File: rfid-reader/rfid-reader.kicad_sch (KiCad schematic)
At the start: 14 parts, among them U1 ATmega1284-P, U2 keypad, U3 Interface_RFID_SPI

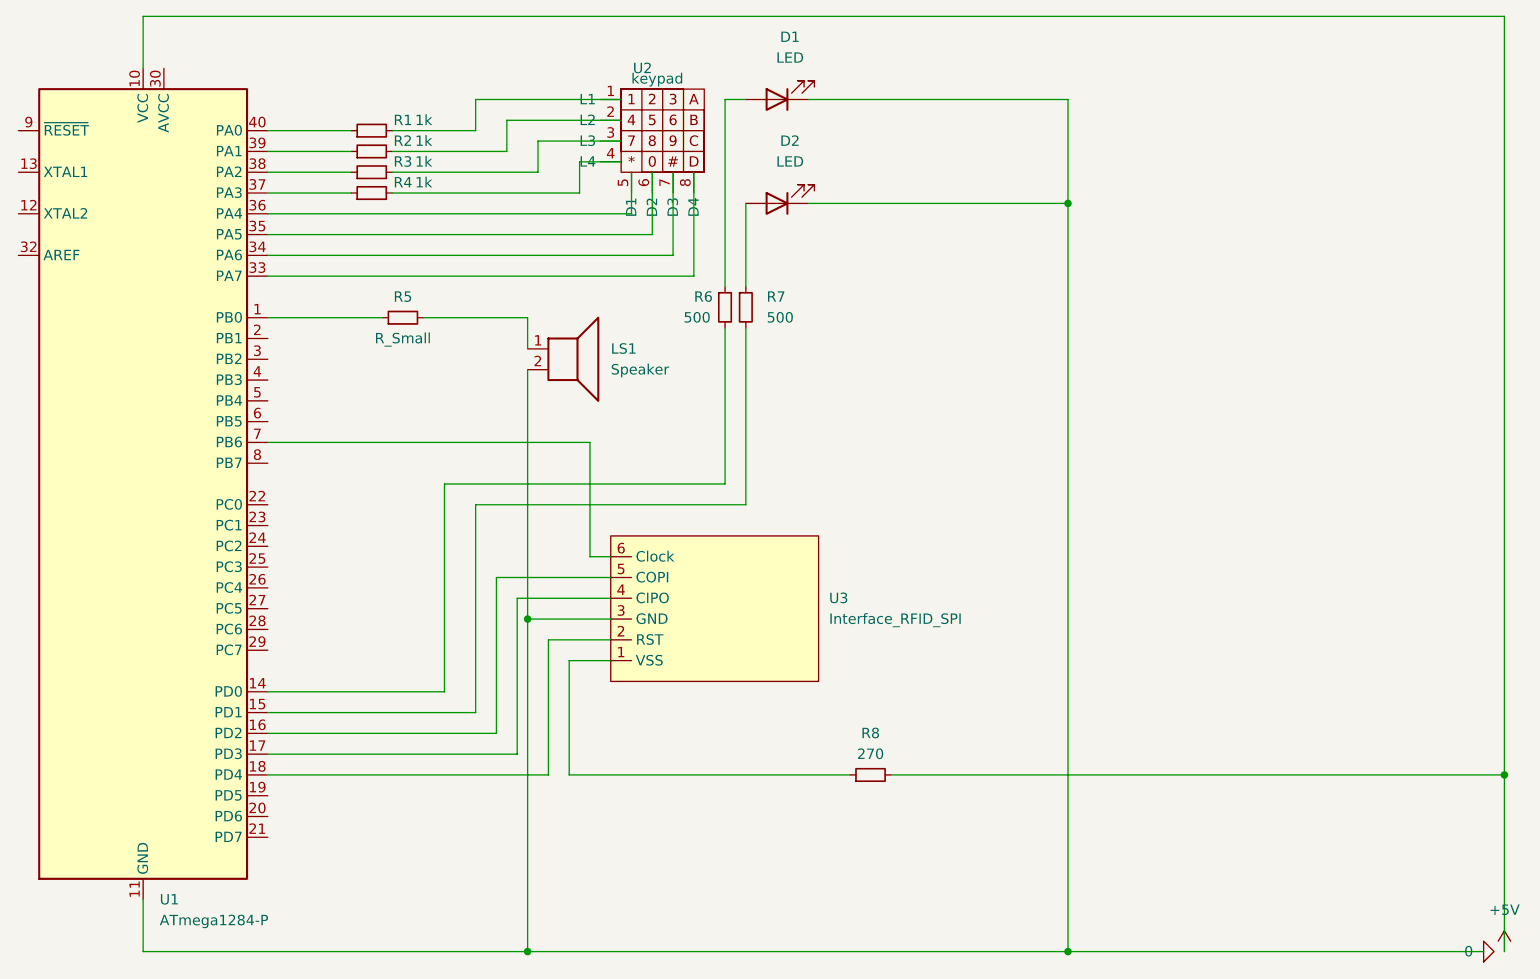
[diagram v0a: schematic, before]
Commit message: Pin configuration is now accurate to reality
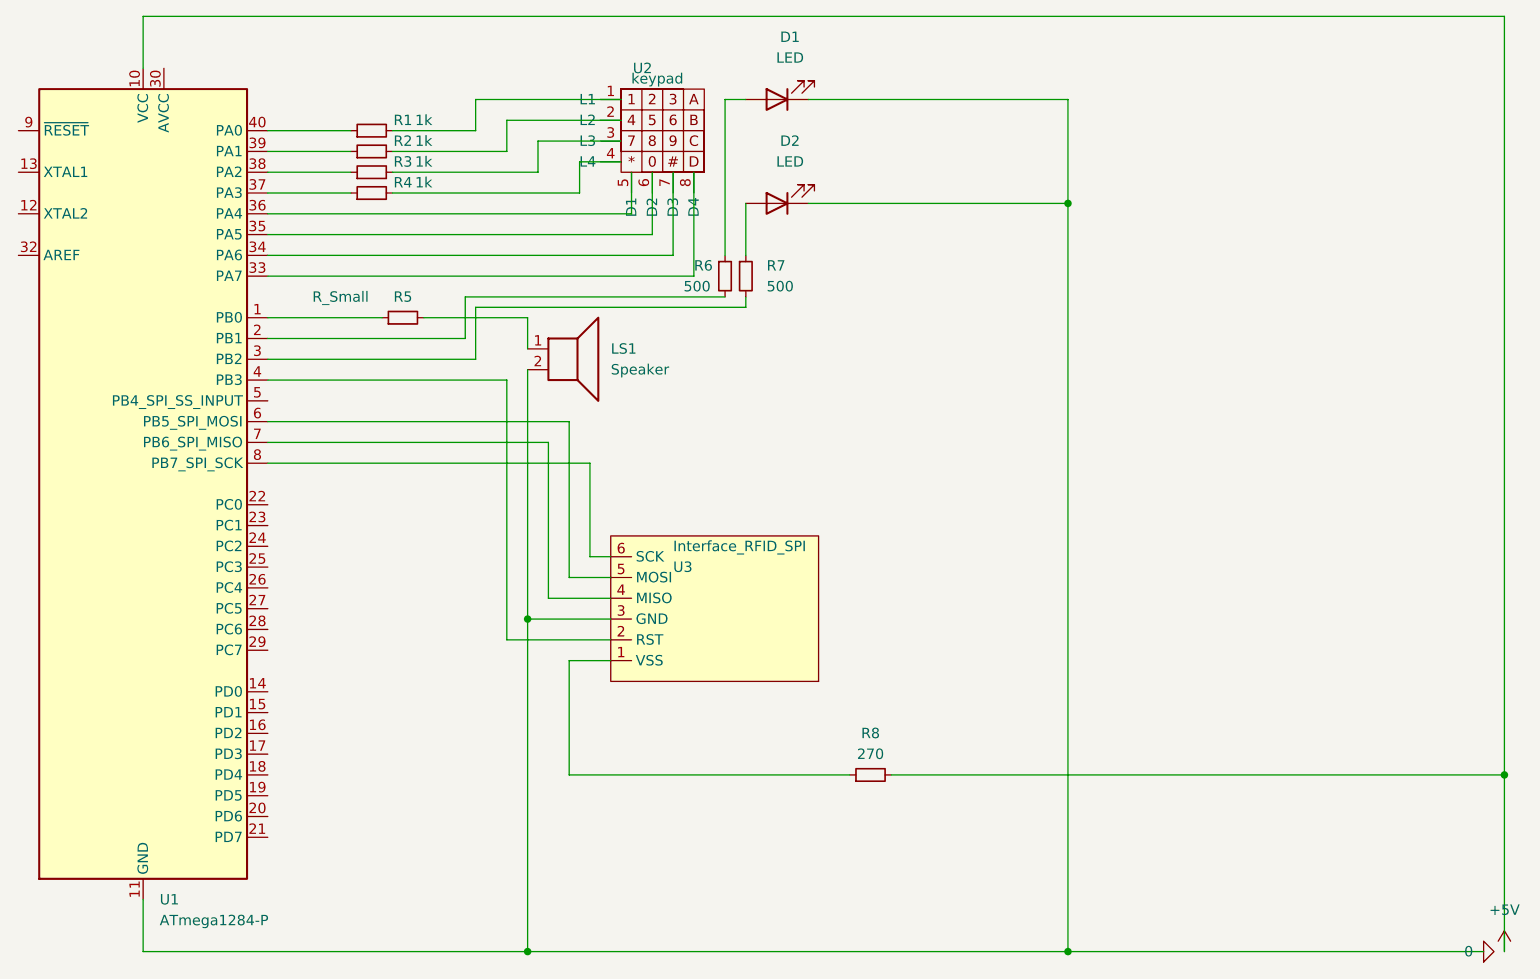
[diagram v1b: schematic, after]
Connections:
- net at U3.2 (RST): now also U1.4 (PB3); no longer U1.18 (PD4)
- net at U3.4 (MISO): now also U1.7 (PB6_SPI_MISO); no longer U1.17 (PD3)
- net at U3.5 (MOSI): now also U1.6 (PB5_SPI_MOSI); no longer U1.16 (PD2)
- net at U3.6 (SCK): now also U1.8 (PB7_SPI_SCK); no longer U1.7 (PB6)
- net at R6.2: now also U1.2 (PB1); no longer U1.14 (PD0)
- net at U1.15 (PD1): no longer R7.2
- net at U1.3 (PB2): now also R7.2
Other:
- moved on the sheet: R6, R7

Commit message: Removed resistors from keypad circuit
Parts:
- removed R1, R2, R3, R4: 1k, symbol Device:R_Small
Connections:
- net at U2.1 (L1): now also U1.40 (PA0)
- net at U2.2 (L2): now also U1.39 (PA1)
- net at U2.3 (L3): now also U1.38 (PA2)
- net at U2.4 (L4): now also U1.37 (PA3)
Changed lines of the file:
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@@
-    (stroke (width 0) (type default) (color 0 0 0 0))
-  )
-  (wire (pts (xy 64.77 34.29) (xy 74.93 34.29))
     (stroke (width 0) (type default) (color 0 0 0 0))
   )
@@
     (stroke (width 0) (type default) (color 0 0 0 0))
   )
-  (wire (pts (xy 80.01 34.29) (xy 93.98 34.29))
+  (wire (pts (xy 64.77 34.29) (xy 93.98 34.29))
     (stroke (width 0) (type default) (color 0 0 0 0))
   )
@@
     (stroke (width 0) (type default) (color 0 0 0 0))
   )
-  (wire (pts (xy 80.01 31.75) (xy 90.17 31.75))
+  (wire (pts (xy 64.77 31.75) (xy 90.17 31.75))
     (stroke (width 0) (type default) (color 0 0 0 0))
   )
@@
     (stroke (width 0) (type default) (color 0 0 0 0))
   )
-  (wire (pts (xy 64.77 31.75) (xy 74.93 31.75))
-    (stroke (width 0) (type default) (color 0 0 0 0))
-  )
   (wire (pts (xy 64.77 44.45) (xy 111.76 44.45))
     (stroke (width 0) (type default) (color 0 0 0 0))
@@
     (stroke (width 0) (type default) (color 0 0 0 0))
   )
-  (wire (pts (xy 80.01 36.83) (xy 97.79 36.83))
+  (wire (pts (xy 64.77 36.83) (xy 97.79 36.83))
     (stroke (width 0) (type default) (color 0 0 0 0))
   )
@@
     (stroke (width 0) (type default) (color 0 0 0 0))
   )
-  (wire (pts (xy 80.01 39.37) (xy 102.87 39.37))
+  (wire (pts (xy 64.77 39.37) (xy 102.87 39.37))
     (stroke (width 0) (type default) (color 0 0 0 0))
   )
@@
     (stroke (width 0) (type default) (color 0 0 0 0))
   )
-  (wire (pts (xy 64.77 36.83) (xy 74.93 36.83))
-    (stroke (width 0) (type default) (color 0 0 0 0))
-  )
   (wire (pts (xy 106.68 93.98) (xy 93.98 93.98))
     (stroke (width 0) (type default) (color 0 0 0 0))
   )
   (wire (pts (xy 162.56 40.64) (xy 162.56 132.08))
-    (stroke (width 0) (type default) (color 0 0 0 0))
-  )
-  (wire (pts (xy 64.77 39.37) (xy 74.93 39.37))
     (stroke (width 0) (type default) (color 0 0 0 0))
   )
@@
     (pin "9")
   )
-  (symbol (lib_id "Device:R_Small") (at 77.47 39.37 90) (unit 1)
-    (in_bom yes) (on_board yes)
-    (property "Reference" "R4" (id 0) (at 81.28 38.1 90))
-    (property "Value" "1k" (id 1) (at 83.82 38.1 90))
-    (property "Footprint" "" (id 2) (at 77.47 39.37 0)
-      (effects (font (size 1.27 1.27)) hide)
-    )
-    (property "Datasheet" "~" (id 3) (at 77.47 39.37 0)
-      (effects (font (size 1.27 1.27)) hide)
-    )
-    (pin "1")
-    (pin "2")
-  )
-  (symbol (lib_id "Device:R_Small") (at 77.47 34.29 90) (unit 1)
-    (in_bom yes) (on_board yes)
-    (property "Reference" "R2" (id 0) (at 81.28 33.02 90))
-    (property "Value" "1k" (id 1) (at 83.82 33.02 90))
-    (property "Footprint" "" (id 2) (at 77.47 34.29 0)
-      (effects (font (size 1.27 1.27)) hide)
-    )
-    (property "Datasheet" "~" (id 3) (at 77.47 34.29 0)
-      (effects (font (size 1.27 1.27)) hide)
-    )
-    (pin "1")
-    (pin "2")
-  )
   (symbol (lib_id "Device:LED") (at 127 27.94 180) (unit 1)
     (in_bom yes) (on_board yes) (fields_autoplaced)
@@
     (pin "2")
   )
-  (symbol (lib_id "Device:R_Small") (at 77.47 31.75 90) (unit 1)
-    (in_bom yes) (on_board yes)
-    (property "Reference" "R1" (id 0) (at 81.28 30.48 90))
-    (property "Value" "1k" (id 1) (at 83.82 30.48 90))
-    (property "Footprint" "" (id 2) (at 77.47 31.75 0)
-      (effects (font (size 1.27 1.27)) hide)
-    )
-    (property "Datasheet" "~" (id 3) (at 77.47 31.75 0)
-      (effects (font (size 1.27 1.27)) hide)
-    )
-    (pin "1")
-    (pin "2")
-  )
   (symbol (lib_id "Device:R_Small") (at 123.19 49.53 0) (unit 1)
     (in_bom yes) (on_board yes) (fields_autoplaced)
@@
     )
     (property "Datasheet" "~" (id 3) (at 123.19 49.53 0)
-      (effects (font (size 1.27 1.27)) hide)
-    )
-    (pin "1")
-    (pin "2")
-  )
-  (symbol (lib_id "Device:R_Small") (at 77.47 36.83 90) (unit 1)
-    (in_bom yes) (on_board yes)
-    (property "Reference" "R3" (id 0) (at 81.28 35.56 90))
-    (property "Value" "1k" (id 1) (at 83.82 35.56 90))
-    (property "Footprint" "" (id 2) (at 77.47 36.83 0)
-      (effects (font (size 1.27 1.27)) hide)
-    )
-    (property "Datasheet" "~" (id 3) (at 77.47 36.83 0)
       (effects (font (size 1.27 1.27)) hide)
     )
@@
       (reference "LS1") (unit 1) (value "Speaker") (footprint "")
     )
-    (path "/ab9b8f6b-95f8-4720-b647-ad34a41fbc87"
-      (reference "R1") (unit 1) (value "1k") (footprint "")
-    )
-    (path "/878ab29b-1284-4f83-a1ea-fdccb65aaae7"
-      (reference "R2") (unit 1) (value "1k") (footprint "")
-    )
-    (path "/d2849447-f67a-4ba8-b3e1-f960c27f713e"
-      (reference "R3") (unit 1) (value "1k") (footprint "")
-    )
-    (path "/6c66599f-4a2f-49ff-a7d3-24caa6225726"
-      (reference "R4") (unit 1) (value "1k") (footprint "")
-    )
     (path "/a8919c86-07ad-486d-bb41-d6c59515ee92"
